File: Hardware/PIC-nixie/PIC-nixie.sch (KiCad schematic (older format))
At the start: 54 parts, among them J1 DX07S024WJ3R400, J2 Conn_01x20_Female, M1 TP5335, M2 TP5335, M3 TP5335, M4 TP5335, Q1 PMBTA42,185, Q2 PMBTA42,185, Q3 PMBTA42,185, Q4 PMBTA42,185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

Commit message: add battery backup for power failures
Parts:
- removed C11: 2.2u film, external:ECQ-E2275JB, symbol Device:C
- removed SW1: SW_SPST, external:SW_TL3301SPF260QG, symbol Switch:SW_SPST
- added BT1: rjd2032C1, Battery:BatteryHolder_Keystone_1060_1x2032, symbol Device:Battery_Cell
- added C13, C14: 4.7u, Capacitor_SMD:C_0805_2012Metric_Pad1.15x1.40mm_HandSolder, symbol Device:C
- added D2: BAT54C, Package_TO_SOT_SMD:SOT-23, symbol Diode:BAT54C
- added R2: 28k, Resistor_SMD:R_0805_2012Metric_Pad1.15x1.40mm_HandSolder, symbol Device:R_US
- added U8: MCP73832-2-OT, Package_TO_SOT_SMD:SOT-23-5, symbol Battery_Management:MCP73832-2-OT
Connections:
- net GND: now also BT1.2 (-), C13.2, C14.2, R2.2, U8.2 (VSS)
- net VCC: now also C13.1, D2.1, U8.4 (VDD); no longer C1.1, C4.1, R1.1, U1.14 (VDD), U6.1 (VIN), U6.3 (CE)
- new net: C1.1, C4.1, D2.3, R1.1, U1.14 (VDD), U6.1 (VIN), U6.3 (CE)
- new net: BT1.1 (+), C14.1, D2.2, U8.3 (VBAT)
- new net: R2.1, U8.5 (PROG)
- no-connect marks 23 -> 25
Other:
- note added: "R10 value is sensitive. R6-R9 can be tuned for brightness.\nPIC16F54 needs to be configured in XT mode\nVdrive is nominally 170V"
- note removed: "R10 value is sensitive. R6-R9 can be tuned for brightness.\nPIC16F54 needs to be configured in XT mode; the clock voltage is too low for HS mode\nVdrive is nominally 170V"

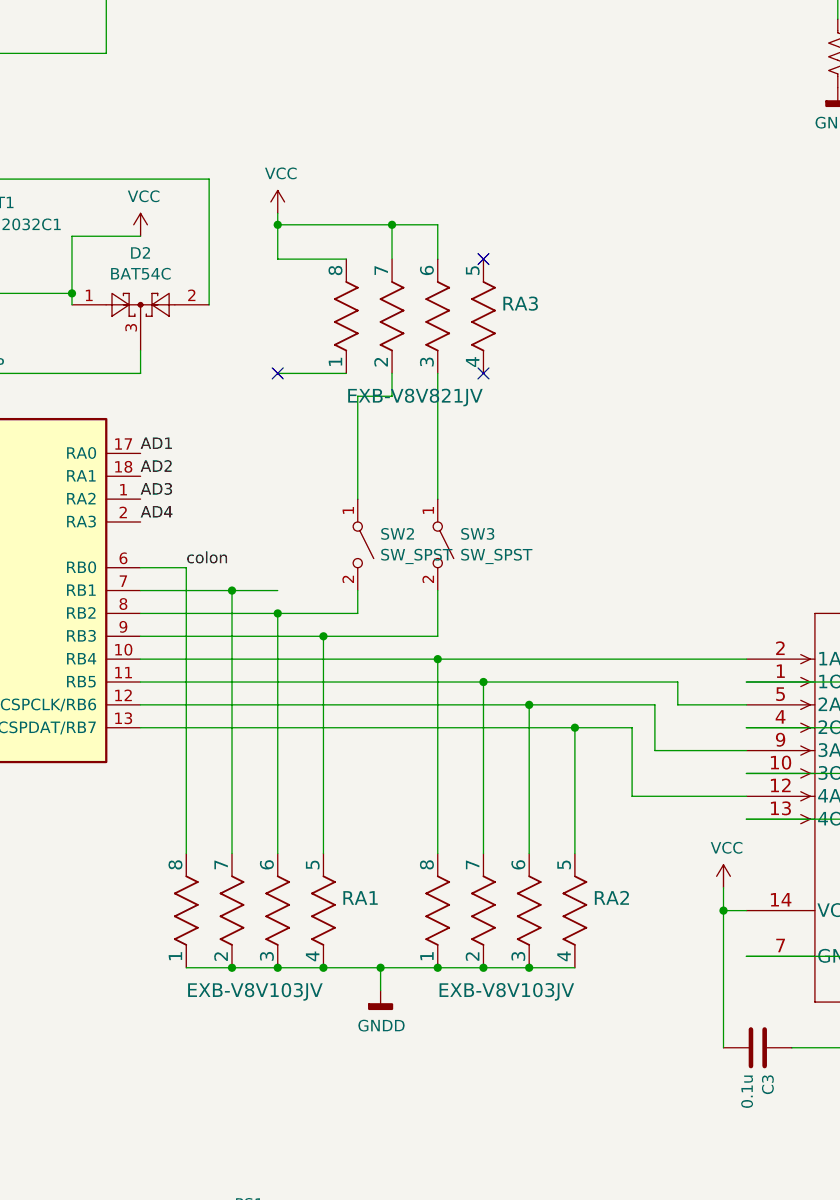
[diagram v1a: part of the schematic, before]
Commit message: update 3D view, add figures
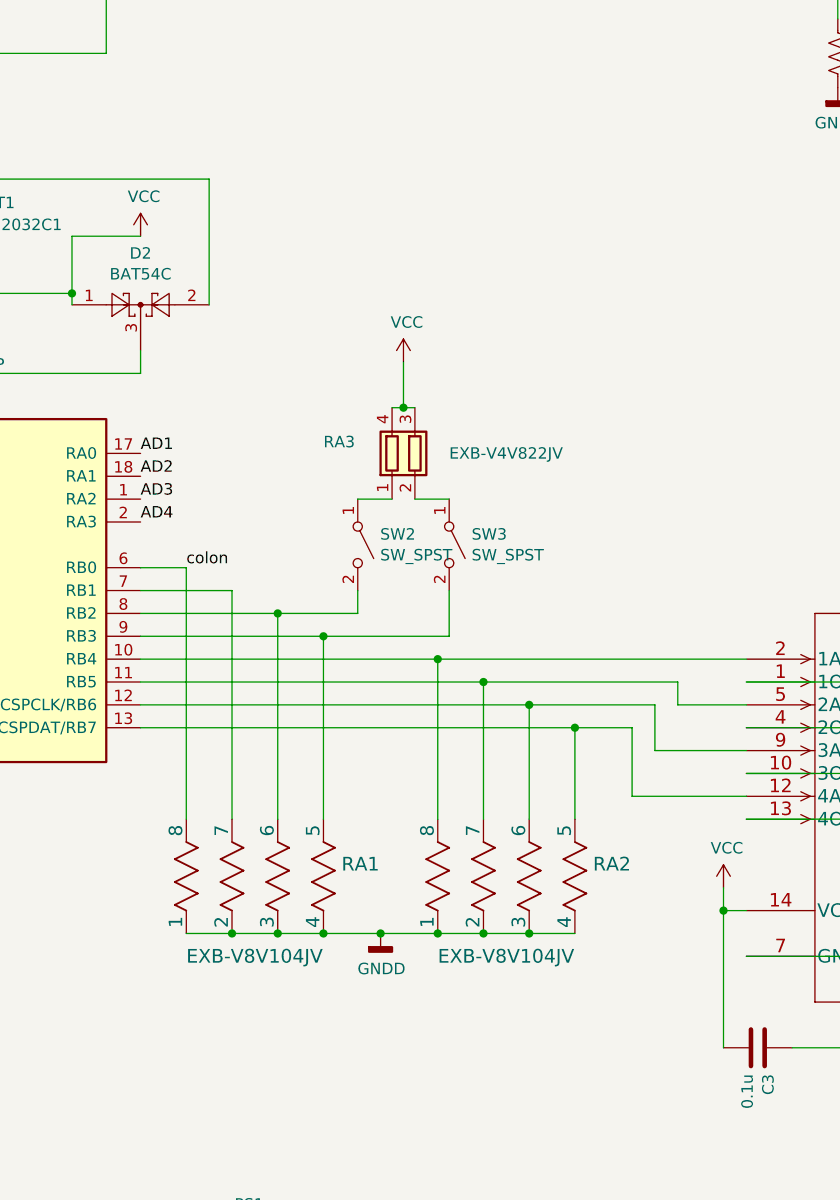
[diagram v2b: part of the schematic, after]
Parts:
- removed RA3: EXB-V8V821JV, Resistor_SMD:R_Array_Convex_4x0603, symbol resarray:EXB-V8V105JV
- added RA3: EXB-V4V822JV, Resistor_SMD:R_Array_Convex_2x0603, symbol Device:R_Pack02
- RA1, RA2: value EXB-V8V103JV -> EXB-V8V104JV
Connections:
- net VCC: now also RA3.3 (R2.2), RA3.4 (R1.2)
- net at SW2.1 (A): now also RA3.1 (R1.1)
- net at SW3.1 (A): now also RA3.2 (R2.1)
- no-connect marks 25 -> 22
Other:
- moved on the sheet: RA1, RA2, SW3
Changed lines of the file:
@@
 $EndDescr
-$Comp
-L MCU_Microchip_PIC16:PIC16F54-IP U1
-U 1 1 607CE7CC
-P 5500 5800
-F 0 "U1" H 5500 6881 50  0000 C CNN
-F 1 "PIC16F54-IP" H 5500 6790 50  0000 C CNN
-F 2 "Package_DIP:DIP-18_W7.62mm_Socket" H 5500 5800 50  0001 C CIN
-F 3 "http://ww1.microchip.com/downloads/en/DeviceDoc/41213D.pdf" H 5500 5800 50  0001 C CNN
-	1    5500 5800
-	1    0    0    -1
-$EndComp
 $Comp
 L eec:74LVC2G80 U5
@@
 Wire Wire Line
 	4400 6300 4400 6400
-Wire Wire Line
-	5500 4850 5500 4900
-Connection ~ 5500 4900
-Wire Wire Line
-	5500 4900 5500 6300
 $Comp
 L Switch:SW_SPST SW2
@@
 L Switch:SW_SPST SW3
 U 1 1 60815501
-P 7600 5600
-F 0 "SW3" V 7554 5698 50  0000 L CNN
-F 1 "SW_SPST" V 7645 5698 50  0000 L CNN
-F 2 "external:SW_TL3301SPF260QG" H 7600 5600 50  0001 C CNN
-F 3 "~" H 7600 5600 50  0001 C CNN
-	1    7600 5600
+P 7650 5600
+F 0 "SW3" V 7604 5698 50  0000 L CNN
+F 1 "SW_SPST" V 7695 5698 50  0000 L CNN
+F 2 "external:SW_TL3301SPF260QG" H 7650 5600 50  0001 C CNN
+F 3 "~" H 7650 5600 50  0001 C CNN
+	1    7650 5600
 	0    1    1    0
 $EndComp
@@
 L power:VCC #PWR0110
 U 1 1 608176E7
-P 6900 4150
-F 0 "#PWR0110" H 6900 4000 50  0001 C CNN
-F 1 "VCC" H 6915 4323 50  0000 C CNN
-F 2 "" H 6900 4150 50  0001 C CNN
-F 3 "" H 6900 4150 50  0001 C CNN
-	1    6900 4150
-	1    0    0    -1
-$EndComp
-Wire Wire Line
-	7250 4950 7250 5400
-Wire Wire Line
-	6900 4150 6900 4200
-Connection ~ 6900 4200
-Wire Wire Line
-	7600 5800 7600 6000
-Wire Wire Line
-	7600 4200 7400 4200
+P 7450 4800
+F 0 "#PWR0110" H 7450 4650 50  0001 C CNN
+F 1 "VCC" H 7465 4973 50  0000 C CNN
+F 2 "" H 7450 4800 50  0001 C CNN
+F 3 "" H 7450 4800 50  0001 C CNN
+	1    7450 4800
+	1    0    0    -1
+$EndComp
+Wire Wire Line
+	7650 5800 7650 6000
 $Comp
 L hct125d:74HCT125D U3
@@
 $EndComp
 Wire Wire Line
-	6300 6400 8200 6400
-Wire Wire Line
-	8450 6400 8450 6700
-Wire Wire Line
 	8550 6300 8550 6500
 Wire Wire Line
@@
 Wire Wire Line
 	8950 6300 8650 6300
-Wire Wire Line
-	8650 6300 8650 6200
 Wire Wire Line
 	8950 6800 9500 6800
@@
 Wire Wire Line
 	14750 3950 14750 3750
-$Comp
-L resarray:EXB-V8V105JV RA2
-U 1 1 60AD8039
-P 7600 7450
-F 0 "RA2" V 7903 6771 60  0000 R CNN
-F 1 "EXB-V8V103JV" V 7500 7450 60  0000 R CNN
-F 2 "Resistor_SMD:R_Array_Convex_4x0603" H 7850 7115 60  0001 C CNN
-F 3 "" H 7600 7450 60  0000 C CNN
-	1    7600 7450
-	0    -1   -1   0
-$EndComp
 Wire Wire Line
 	8450 6700 8950 6700
-Wire Wire Line
-	6300 6300 8000 6300
-Wire Wire Line
-	6300 6200 7800 6200
-Wire Wire Line
-	6300 6100 7600 6100
-Wire Wire Line
-	7600 6950 7600 6100
-Connection ~ 7600 6100
-Wire Wire Line
-	7600 6100 8950 6100
-Wire Wire Line
-	7800 6950 7800 6200
-Connection ~ 7800 6200
-Wire Wire Line
-	7800 6200 8650 6200
-Wire Wire Line
-	8000 6950 8000 6300
-Connection ~ 8000 6300
-Wire Wire Line
-	8000 6300 8550 6300
-Wire Wire Line
-	8200 6950 8200 6400
-Connection ~ 8200 6400
-Wire Wire Line
-	8200 6400 8450 6400
-Wire Wire Line
-	8200 7450 8000 7450
-Wire Wire Line
-	7800 7450 8000 7450
-Connection ~ 8000 7450
-Wire Wire Line
-	7800 7450 7600 7450
-Connection ~ 7800 7450
-$Comp
-L resarray:EXB-V8V105JV RA1
-U 1 1 60B1D18D
-P 6500 7450
-F 0 "RA1" V 6803 6771 60  0000 R CNN
-F 1 "EXB-V8V103JV" V 6400 7450 60  0000 R CNN
-F 2 "Resistor_SMD:R_Array_Convex_4x0603" H 6750 7115 60  0001 C CNN
-F 3 "" H 6500 7450 60  0000 C CNN
-	1    6500 7450
-	0    -1   -1   0
-$EndComp
-Wire Wire Line
-	6300 5900 6900 5900
-Wire Wire Line
-	6300 6000 7100 6000
-Wire Wire Line
-	7100 6950 7100 6000
-Connection ~ 7100 6000
-Wire Wire Line
-	7100 6000 7600 6000
-Wire Wire Line
-	6900 6950 6900 5900
-Connection ~ 6900 5900
-Wire Wire Line
-	6900 5900 7250 5900
-Wire Wire Line
-	6300 5800 6700 5800
-Wire Wire Line
-	6700 6950 6700 5800
-Connection ~ 6700 5800
-Wire Wire Line
-	6700 5800 6900 5800
-$Comp
-L power:GNDD #PWR0123
-U 1 1 60BB1523
-P 7350 7550
-F 0 "#PWR0123" H 7350 7300 50  0001 C CNN
-F 1 "GNDD" H 7354 7395 50  0000 C CNN
-F 2 "" H 7350 7550 50  0001 C CNN
-F 3 "" H 7350 7550 50  0001 C CNN
-	1    7350 7550
-	1    0    0    -1
-$EndComp
-Wire Wire Line
-	7100 7450 6900 7450
-Wire Wire Line
-	6900 7450 6700 7450
-Connection ~ 6900 7450
-Wire Wire Line
-	6700 7450 6500 7450
-Connection ~ 6700 7450
-Wire Wire Line
-	7600 7450 7350 7450
-Connection ~ 7600 7450
-Connection ~ 7100 7450
-Wire Wire Line
-	7350 7550 7350 7450
-Connection ~ 7350 7450
-Wire Wire Line
-	7350 7450 7100 7450
 Connection ~ 12600 7300
 Text Label 12650 7500 0    50   ~ 0
@@
 Wire Wire Line
 	13550 7300 13750 7300
-Wire Wire Line
-	6500 6950 6500 5700
 Wire Wire Line
 	6300 5700 6500 5700
@@
 $EndComp
 $Comp
-L resarray:EXB-V8V105JV RA3
-U 1 1 61A850D9
-P 7200 4850
-F 0 "RA3" V 7503 4171 60  0000 R CNN
-F 1 "EXB-V8V821JV" V 7100 4850 60  0000 R CNN
-F 2 "Resistor_SMD:R_Array_Convex_4x0603" H 7450 4515 60  0001 C CNN
-F 3 "" H 7200 4850 60  0000 C CNN
-	1    7200 4850
-	0    -1   -1   0
-$EndComp
-Wire Wire Line
-	7250 4950 7400 4950
-Wire Wire Line
-	7400 4950 7400 4850
-Wire Wire Line
-	7600 4850 7600 5400
-Wire Wire Line
-	6900 4850 7200 4850
-Wire Wire Line
-	7400 4350 7400 4200
-Connection ~ 7400 4200
-Wire Wire Line
-	7600 4200 7600 4350
-Wire Wire Line
-	6900 4350 7200 4350
-Wire Wire Line
-	6900 4200 6900 4350
-Wire Wire Line
-	6900 4200 7400 4200
-NoConn ~ 7800 4350
-NoConn ~ 7800 4850
-$Comp
 L Connector:Conn_01x20_Female J2
 U 1 1 617CAFFA
@@
 	6000 4500 6000 4550
 NoConn ~ 4850 4200
-NoConn ~ 6900 4850
+$Comp
+L resarray:EXB-V8V105JV RA2
+U 1 1 60AD8039
+P 7600 7300
+F 0 "RA2" V 7903 6621 60  0000 R CNN
+F 1 "EXB-V8V104JV" V 7500 7300 60  0000 R CNN
+F 2 "Resistor_SMD:R_Array_Convex_4x0603" H 7850 6965 60  0001 C CNN
+F 3 "" H 7600 7300 60  0000 C CNN
+	1    7600 7300
+	0    -1   -1   0
+$EndComp
+Connection ~ 7600 7300
+Wire Wire Line
+	7800 7300 7600 7300
+Wire Wire Line
+	7600 7300 7350 7300
+Connection ~ 7800 7300
+Wire Wire Line
+	7800 7300 8000 7300
+Connection ~ 8000 7300
+Wire Wire Line
+	8200 7300 8000 7300
+Wire Wire Line
+	5500 4850 5500 4900
+Connection ~ 5500 4900
+$Comp
+L MCU_Microchip_PIC16:PIC16F54-IP U1
+U 1 1 607CE7CC
+P 5500 5800
+F 0 "U1" H 5500 6881 50  0000 C CNN
+F 1 "PIC16F54-IP" H 5500 6790 50  0000 C CNN
+F 2 "Package_DIP:DIP-18_W7.62mm_Socket" H 5500 5800 50  0001 C CIN
+F 3 "http://ww1.microchip.com/downloads/en/DeviceDoc/41213D.pdf" H 5500 5800 50  0001 C CNN
+	1    5500 5800
+	1    0    0    -1
+$EndComp
+Wire Wire Line
+	5500 4900 5500 6300
+$Comp
+L power:GNDD #PWR0145
+U 1 1 632E4D0D
+P 7350 7300
+F 0 "#PWR0145" H 7350 7050 50  0001 C CNN
+F 1 "GNDD" H 7354 7145 50  0000 C CNN
+F 2 "" H 7350 7300 50  0001 C CNN
+F 3 "" H 7350 7300 50  0001 C CNN
+	1    7350 7300
+	1    0    0    -1
+$EndComp
+Wire Wire Line
+	6300 5900 6900 5900
+Wire Wire Line
+	8650 6200 8650 6300
+Wire Wire Line
+	8450 6400 8450 6700
+Wire Wire Line
+	7450 4800 7450 5000
+Wire Wire Line
+	7450 5000 7400 5000
+Wire Wire Line
+	7450 5000 7500 5000
+Connection ~ 7450 5000
+Wire Wire Line
+	7400 5400 7250 5400
+Wire Wire Line
+	6300 6000 7100 6000
+Wire Wire Line
+	7500 5400 7650 5400
+$Comp
+L Device:R_Pack02 RA3
+U 1 1 632E05AC
+P 7500 5200
+F 0 "RA3" H 7100 5250 50  0000 L CNN
+F 1 "EXB-V4V822JV" H 7650 5200 50  0000 L CNN
+F 2 "Resistor_SMD:R_Array_Convex_2x0603" V 7675 5200 50  0001 C CNN
+F 3 "~" H 7500 5200 50  0001 C CNN
+	1    7500 5200
+	1    0    0    -1
+$EndComp
+Wire Wire Line
+	7350 7300 7100 7300
+Connection ~ 7100 7300
+Wire Wire Line
+	7100 7300 6900 7300
+Connection ~ 6900 7300
+Wire Wire Line
+	6700 7300 6500 7300
+Wire Wire Line
+	6900 7300 6700 7300
+Connection ~ 6700 7300
+$Comp
+L resarray:EXB-V8V105JV RA1
+U 1 1 60B1D18D
+P 6500 7300
+F 0 "RA1" V 6803 6621 60  0000 R CNN
+F 1 "EXB-V8V104JV" V 6400 7300 60  0000 R CNN
+F 2 "Resistor_SMD:R_Array_Convex_4x0603" H 6750 6965 60  0001 C CNN
+F 3 "" H 6500 7300 60  0000 C CNN
+	1    6500 7300
+	0    -1   -1   0
+$EndComp
+Connection ~ 7350 7300
+Wire Wire Line
+	6300 6200 7800 6200
+Wire Wire Line
+	6300 6300 8000 6300
+Wire Wire Line
+	6300 6400 8200 6400
+Wire Wire Line
+	6700 6800 6700 5800
+Wire Wire Line
+	6300 5800 6700 5800
+Wire Wire Line
+	6500 6800 6500 5700
+Connection ~ 6900 5900
+Wire Wire Line
+	6900 5900 7250 5900
+Wire Wire Line
+	6900 5900 6900 6800
+Wire Wire Line
+	7100 6800 7100 6000
+Connection ~ 7100 6000
+Wire Wire Line
+	7100 6000 7650 6000
+Wire Wire Line
+	7600 6800 7600 6100
+Wire Wire Line
+	6300 6100 7600 6100
+Connection ~ 7600 6100
+Wire Wire Line
+	7600 6100 8950 6100
+Wire Wire Line
+	7800 6800 7800 6200
+Connection ~ 7800 6200
+Wire Wire Line
+	7800 6200 8650 6200
+Wire Wire Line
+	8000 6800 8000 6300
+Connection ~ 8000 6300
+Wire Wire Line
+	8000 6300 8550 6300
+Wire Wire Line
+	8200 6800 8200 6400
+Connection ~ 8200 6400
+Wire Wire Line
+	8200 6400 8450 6400
 $EndSCHEMATC
